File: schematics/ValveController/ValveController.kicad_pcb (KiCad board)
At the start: 2 copper layers, 81 parts, among them P101 CONN_01X05, P102 CONN_01X03, P103 CONN_01X03, P104 CONN_01X03, P105 CONN_01X02, P106 CONN_01X02, P107 CONN_01X02, P108 CONN_01X02, Q201 BC547, Q202 BC547, Q203 BC547, Q204 BC547, Q205 BC557, Q206 BC547, Q207 BC557, Q208 BC547, Q301 BC547, Q302 BC547, Q303 BC547, Q304 BC547, Q305 BC557, Q306 BC547, Q307 BC557, Q308 BC547, Q401 BC547, Q402 BC547, Q403 BC547, Q404 BC547, Q405 BC557, Q406 BC547, Q407 BC557, Q408 BC547, Q501 BC547, Q502 BC547, Q503 BC547, Q504 BC547, Q505 BC557, Q506 BC547, Q507 BC557, Q508 BC547, U101 PCF8574

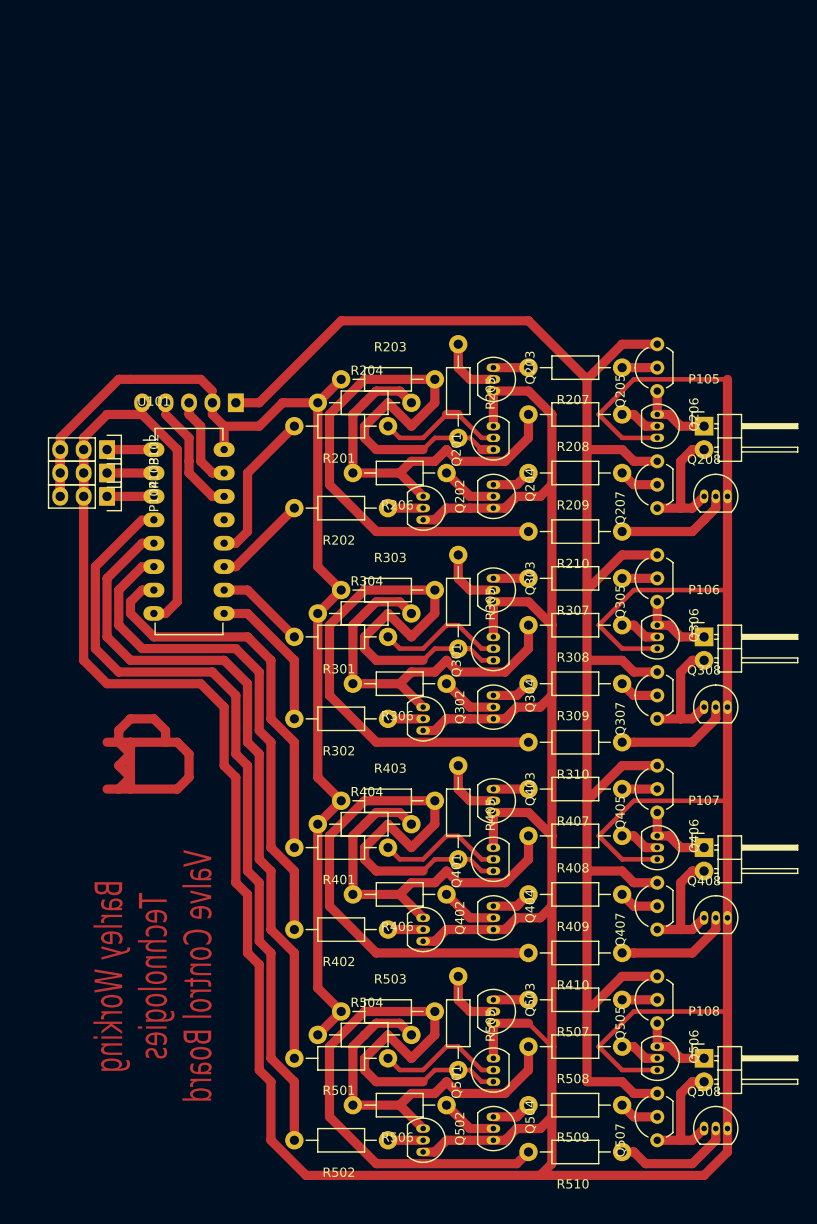
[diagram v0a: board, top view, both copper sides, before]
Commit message: Updated Valve Controller with bigger pads
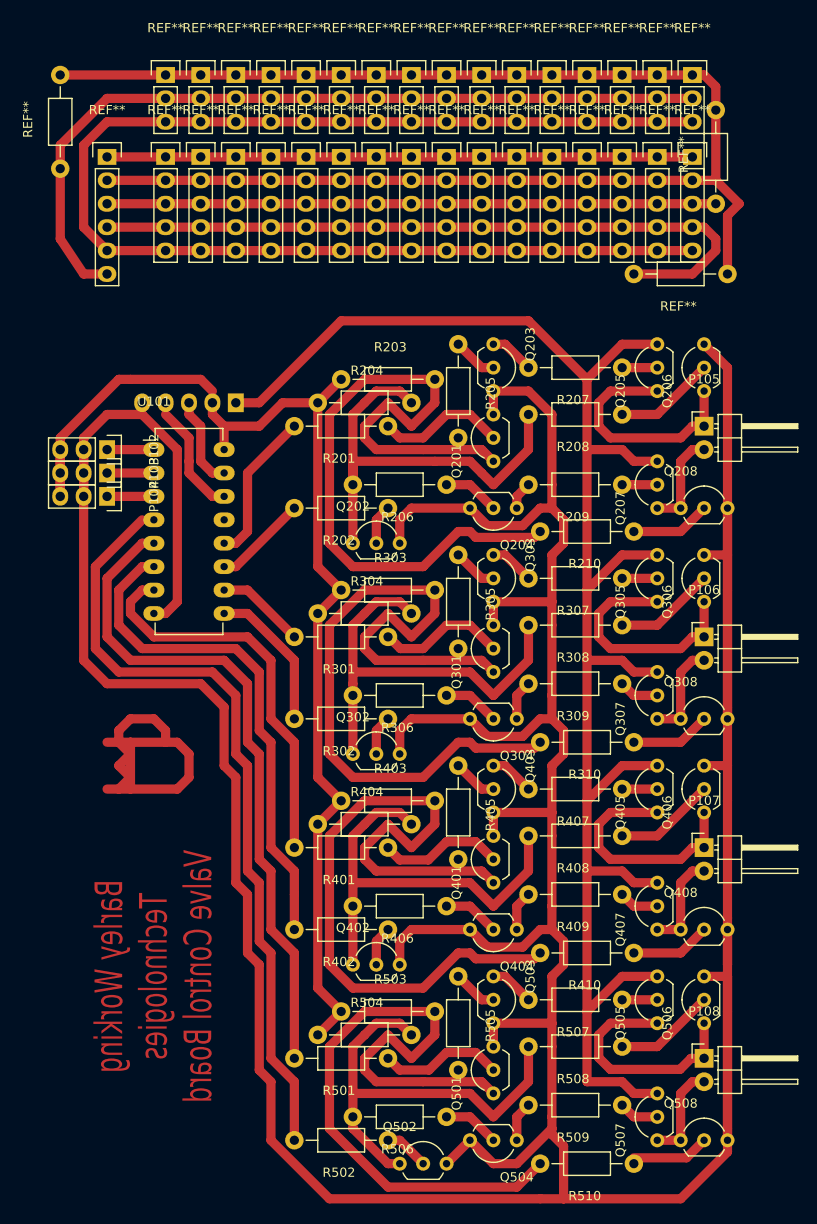
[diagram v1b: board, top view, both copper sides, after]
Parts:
- added REF**: Resistor_Horizontal_RM10mm, Resistors_ThroughHole:Resistor_Horizontal_RM10mm, F.Cu at (50.8, 43.2)
- added REF**: Pin_Header_Straight_1x03, Pin_Headers:Pin_Header_Straight_1x03, F.Cu at (62.2, 38.1)
- added REF**: Pin_Header_Straight_1x03, Pin_Headers:Pin_Header_Straight_1x03, F.Cu at (66.0, 38.1)
- added REF**: Pin_Header_Straight_1x03, Pin_Headers:Pin_Header_Straight_1x03, F.Cu at (69.8, 38.1)
- added REF**: Pin_Header_Straight_1x03, Pin_Headers:Pin_Header_Straight_1x03, F.Cu at (73.7, 38.1)
- added REF**: Pin_Header_Straight_1x03, Pin_Headers:Pin_Header_Straight_1x03, F.Cu at (77.5, 38.1)
- added REF**: Pin_Header_Straight_1x03, Pin_Headers:Pin_Header_Straight_1x03, F.Cu at (81.3, 38.1)
- added REF**: Pin_Header_Straight_1x03, Pin_Headers:Pin_Header_Straight_1x03, F.Cu at (85.1, 38.1)
- added REF**: Pin_Header_Straight_1x05, Pin_Headers:Pin_Header_Straight_1x05, F.Cu at (88.9, 47.0)
- added REF**: Pin_Header_Straight_1x05, Pin_Headers:Pin_Header_Straight_1x05, F.Cu at (92.7, 47.0)
- added REF**: Pin_Header_Straight_1x05, Pin_Headers:Pin_Header_Straight_1x05, F.Cu at (96.5, 47.0)
- added REF**: Resistor_Horizontal_RM10mm, Resistors_ThroughHole:Resistor_Horizontal_RM10mm, F.Cu at (118.1, 59.7)
- added REF**: Pin_Header_Straight_1x05, Pin_Headers:Pin_Header_Straight_1x05, F.Cu at (100.3, 47.0)
- added REF**: Pin_Header_Straight_1x05, Pin_Headers:Pin_Header_Straight_1x05, F.Cu at (104.1, 47.0)
- added REF**: Pin_Header_Straight_1x05, Pin_Headers:Pin_Header_Straight_1x05, F.Cu at (108.0, 47.0)
- added REF**: Pin_Header_Straight_1x05, Pin_Headers:Pin_Header_Straight_1x05, F.Cu at (111.8, 47.0)
- added REF**: Pin_Header_Straight_1x05, Pin_Headers:Pin_Header_Straight_1x05, F.Cu at (115.6, 47.0)
- added REF**: Pin_Header_Straight_1x03, Pin_Headers:Pin_Header_Straight_1x03, F.Cu at (92.7, 38.1)
- added REF**: Pin_Header_Straight_1x03, Pin_Headers:Pin_Header_Straight_1x03, F.Cu at (96.5, 38.1)
- added REF**: Pin_Header_Straight_1x03, Pin_Headers:Pin_Header_Straight_1x03, F.Cu at (100.3, 38.1)
- added REF**: Pin_Header_Straight_1x03, Pin_Headers:Pin_Header_Straight_1x03, F.Cu at (104.1, 38.1)
- added REF**: Pin_Header_Straight_1x03, Pin_Headers:Pin_Header_Straight_1x03, F.Cu at (108.0, 38.1)
- added REF**: Pin_Header_Straight_1x05, Pin_Headers:Pin_Header_Straight_1x05, F.Cu at (62.2, 47.0)
- added REF**: Pin_Header_Straight_1x03, Pin_Headers:Pin_Header_Straight_1x03, F.Cu at (111.8, 38.1)
- added REF**: Pin_Header_Straight_1x03, Pin_Headers:Pin_Header_Straight_1x03, F.Cu at (115.6, 38.1)
- added REF**: Pin_Header_Straight_1x03, Pin_Headers:Pin_Header_Straight_1x03, F.Cu at (119.4, 38.1)
- added REF**: Pin_Header_Straight_1x03, Pin_Headers:Pin_Header_Straight_1x03, F.Cu at (88.9, 38.1)
- added REF**: Pin_Header_Straight_1x05, Pin_Headers:Pin_Header_Straight_1x05, F.Cu at (119.4, 47.0)
- added REF**: Pin_Header_Straight_1x06, Pin_Headers:Pin_Header_Straight_1x06, F.Cu at (55.9, 47.0)
- added REF**: Resistor_Horizontal_RM10mm, Resistors_ThroughHole:Resistor_Horizontal_RM10mm, F.Cu at (121.9, 47.0)
- added REF**: Pin_Header_Straight_1x05, Pin_Headers:Pin_Header_Straight_1x05, F.Cu at (66.0, 47.0)
- added REF**: Pin_Header_Straight_1x05, Pin_Headers:Pin_Header_Straight_1x05, F.Cu at (69.8, 47.0)
- added REF**: Pin_Header_Straight_1x05, Pin_Headers:Pin_Header_Straight_1x05, F.Cu at (73.7, 47.0)
- added REF**: Pin_Header_Straight_1x05, Pin_Headers:Pin_Header_Straight_1x05, F.Cu at (77.5, 47.0)
- added REF**: Pin_Header_Straight_1x05, Pin_Headers:Pin_Header_Straight_1x05, F.Cu at (81.3, 47.0)
- added REF**: Pin_Header_Straight_1x05, Pin_Headers:Pin_Header_Straight_1x05, F.Cu at (85.1, 47.0)
- Q201, Q202, Q203, Q204, Q206, Q208, Q301, Q302, Q303, Q304, Q306, Q308, Q401, Q402, Q403, Q404, Q406, Q408, Q501, Q502, Q503, Q504, Q506, Q508: footprint Housings_TO-92:TO-92_Inline_Narrow_Oval -> Housings_TO-92:TO-92_Inline_Wide
- moved Q202 9.16 mm to (82.5, 88.9), turned to 0 degrees
- moved Q402 9.16 mm to (82.5, 134.6), turned to 0 degrees
- moved Q302 9.16 mm to (82.5, 111.8), turned to 0 degrees
- moved Q206 5.68 mm to (120.7, 72.4), turned to 90 degrees
- moved Q306 5.68 mm to (120.7, 95.2), turned to 90 degrees
- moved Q406 5.68 mm to (120.7, 118.1), turned to 90 degrees
- moved Q506 5.68 mm to (120.7, 141.0), turned to 90 degrees
- moved Q502 4.58 mm to (87.6, 156.2), turned to 0 degrees
- moved Q204 3.59 mm to (100.3, 85.1), turned to 180 degrees
- moved Q304 3.59 mm to (100.3, 108.0), turned to 180 degrees
- moved Q404 3.59 mm to (100.3, 130.8), turned to 180 degrees
- moved Q504 3.59 mm to (100.3, 153.7), turned to 180 degrees
- moved Q208 2.84 mm to (118.1, 85.1)
- moved Q408 2.84 mm to (118.1, 130.8)
- moved Q308 2.84 mm to (118.1, 108.0)
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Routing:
- net (no net): track 42.3 -> 640.2 mm
- net GND: track 547.2 -> 528.3 mm
- net /Valve3/Output_A: track 8.15 -> 25.7 mm
- net /Valve2/Output_A: track 8.15 -> 25.7 mm
- net /Valve1/Output_A: track 8.15 -> 25.7 mm
- net /Valve4/Output_A: track 8.15 -> 25.6 mm
- net Net-(Q201-Pad1): track 74.5 -> 85.1 mm
- net Net-(Q401-Pad1): track 74.5 -> 83.9 mm
- net Net-(Q301-Pad1): track 74.5 -> 83.9 mm
- net Net-(Q202-Pad1): track 42.1 -> 49.9 mm
- net Net-(Q502-Pad1): track 42.1 -> 49.0 mm
- net Net-(Q406-Pad2): track 4.34 -> 11.0 mm
- net Net-(Q306-Pad2): track 4.34 -> 11.0 mm
- net Net-(Q206-Pad2): track 4.34 -> 11.0 mm
- net Net-(Q506-Pad2): track 4.34 -> 11.0 mm
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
